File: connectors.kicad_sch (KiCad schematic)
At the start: 7 parts, among them J1 Conn_01x02, J3 Conn_01x04, J4 Conn_01x04, J5 USB_C_Receptacle_USB2.0

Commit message: WIP routing
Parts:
- D1: value SP0503BAHT -> (none); footprint Package_TO_SOT_SMD:SOT-143 -> (none)
- J1: value Conn_01x02 -> (none); footprint Connector_PinHeader_2.54mm:PinHeader_1x02_P2.54mm_Horizontal -> (none)
- J2: renamed from J5; value USB_C_Receptacle_USB2.0 -> (none); footprint Connector_USB:USB_C_Receptacle_GCT_USB4085 -> (none)
- J3, J4: value Conn_01x04 -> (none); footprint Connector_PinSocket_2.54mm:PinSocket_1x10_P2.54mm_Vertical -> (none)
- R1, R2: value 5.1k -> (none); footprint Resistor_SMD:R_0805_2012Metric -> (none)
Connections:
- net +5V: now also J4.3 (Pin_3); no longer J3.4 (Pin_4)
- net GND: now also J3.10 (Pin_10), J3.4 (Pin_4), J3.8 (Pin_8), J3.9 (Pin_9), J4.4 (Pin_4); no longer J3.5 (Pin_5), J3.6 (Pin_6), J4.6 (Pin_6), J4.7 (Pin_7)
- net I2C.SCL: now also J3.2 (Pin_2), J4.2 (Pin_2); no longer J3.1 (Pin_1)
- net I2C.SDA: now also J3.1 (Pin_1), J4.1 (Pin_1); no longer J3.2 (Pin_2)
- net load_in: now also J3.5 (Pin_5), J3.6 (Pin_6), J3.7 (Pin_7), J4.6 (Pin_6), J4.7 (Pin_7); no longer J4.1 (Pin_1), J4.2 (Pin_2), J4.3 (Pin_3), J4.4 (Pin_4)
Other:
- moved on the sheet: J3

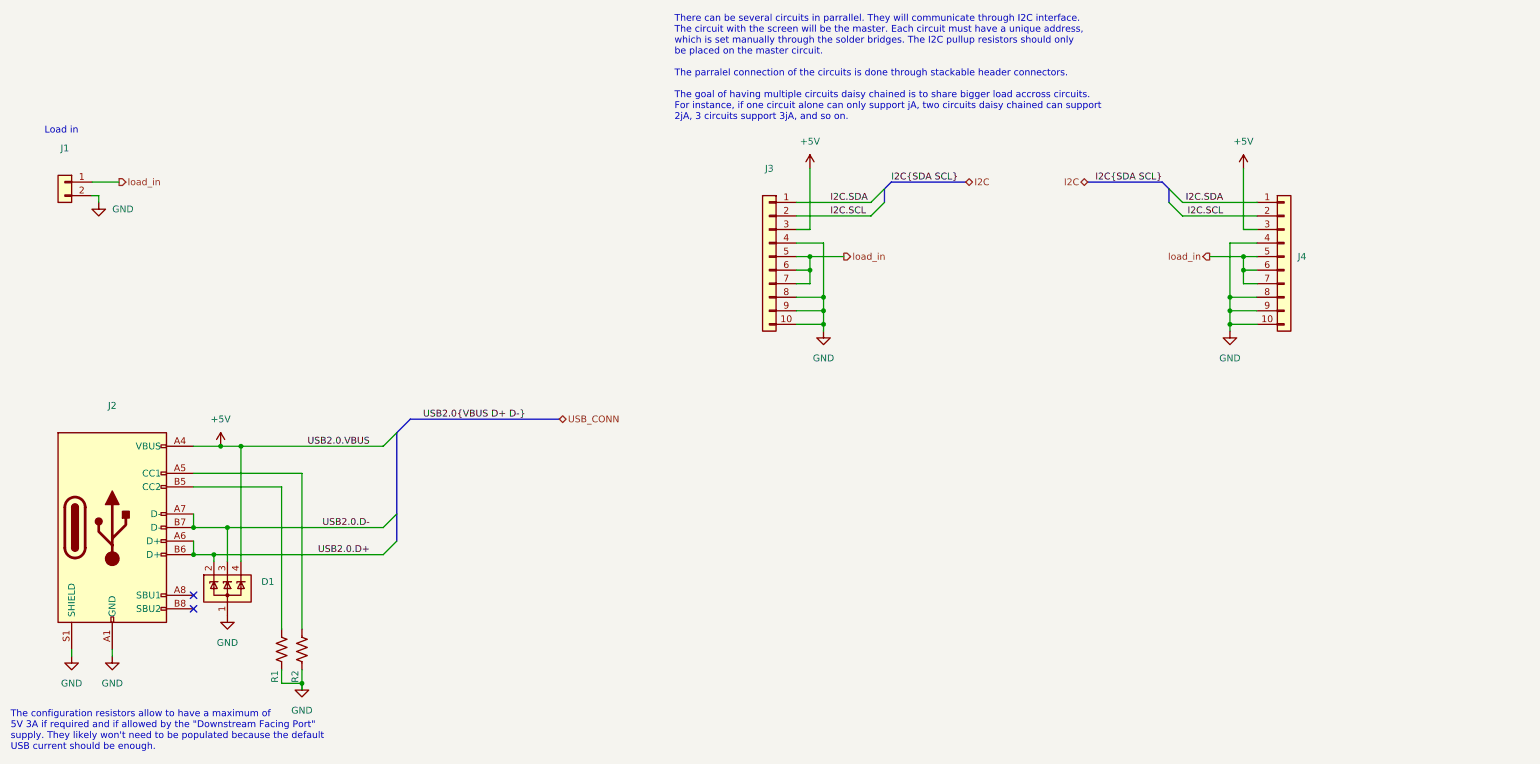
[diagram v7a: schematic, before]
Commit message: Fix and tune differential pair and zones
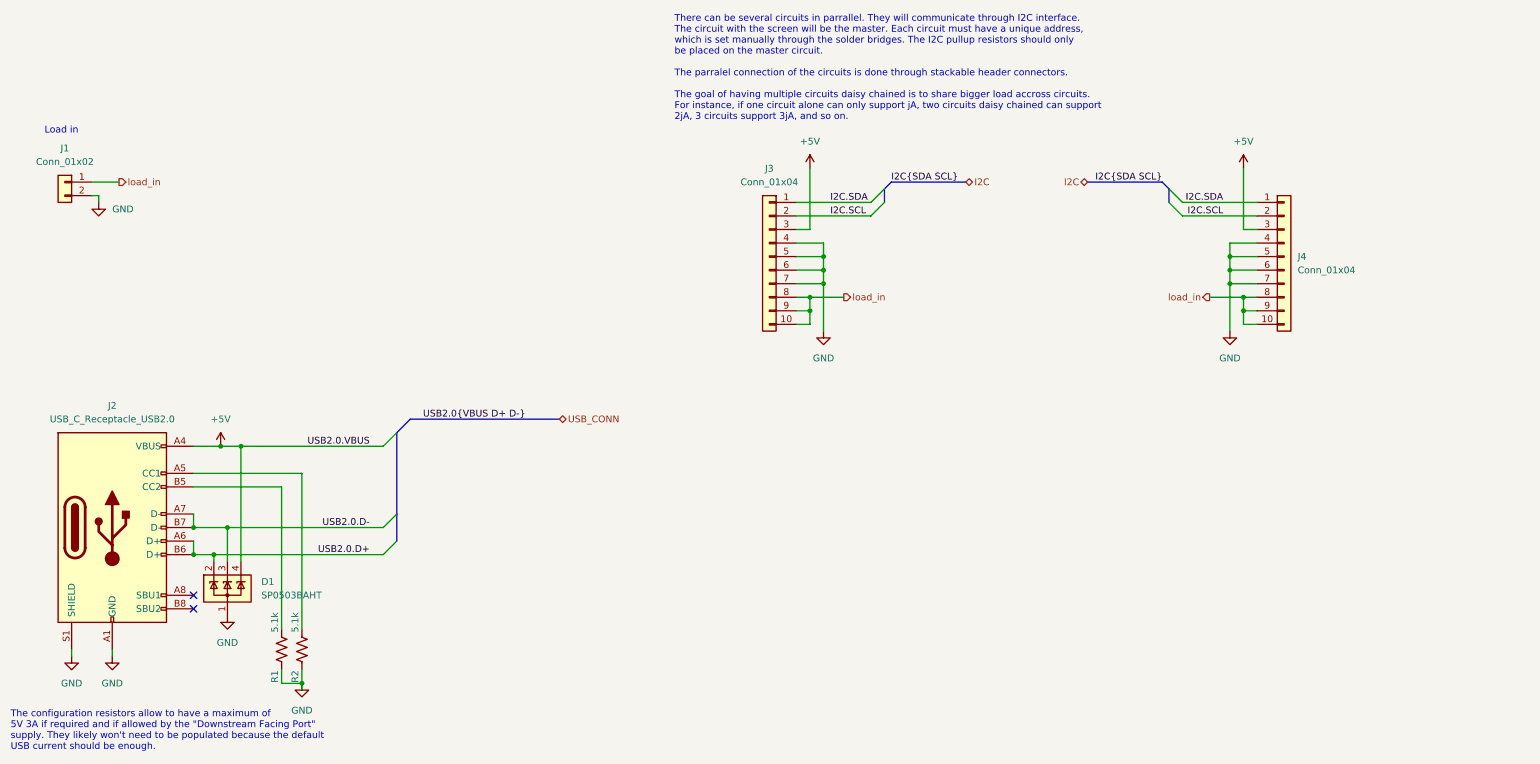
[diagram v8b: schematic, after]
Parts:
- D1: value (none) -> SP0503BAHT; footprint (none) -> Package_TO_SOT_SMD:SOT-143
- J1: value (none) -> Conn_01x02; footprint (none) -> Connector_PinHeader_2.54mm:PinHeader_1x02_P2.54mm_Horizontal
- J2: value (none) -> USB_C_Receptacle_USB2.0; footprint (none) -> Connector_USB:USB_C_Receptacle_GCT_USB4085
- J3, J4: value (none) -> Conn_01x04; footprint (none) -> Connector_PinSocket_2.54mm:PinSocket_1x10_P2.54mm_Vertical
- R1, R2: value (none) -> 5.1k; footprint (none) -> Resistor_SMD:R_0805_2012Metric
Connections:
- net GND: now also J3.5 (Pin_5), J3.6 (Pin_6), J3.7 (Pin_7), J4.5 (Pin_5), J4.6 (Pin_6), J4.7 (Pin_7); no longer J3.10 (Pin_10), J3.8 (Pin_8), J3.9 (Pin_9), J4.10 (Pin_10), J4.8 (Pin_8), J4.9 (Pin_9)
- net load_in: now also J3.10 (Pin_10), J3.8 (Pin_8), J3.9 (Pin_9), J4.10 (Pin_10), J4.8 (Pin_8), J4.9 (Pin_9); no longer J3.5 (Pin_5), J3.6 (Pin_6), J3.7 (Pin_7), J4.5 (Pin_5), J4.6 (Pin_6), J4.7 (Pin_7)
